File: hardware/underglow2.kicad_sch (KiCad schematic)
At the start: 1 part, among them J101 J_Delphi_Sicma_24

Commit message: Schematic progress
Signed-off-by: Connor Rigby <connorr@hey.com>
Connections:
- net CAN_H renamed CAN/CAN_H
- net CAN_L renamed CAN/CAN_L
- net DI_1 renamed Digital Input/DI_1
- net DI_2 renamed Digital Input/DI_2
- net DI_3 renamed Digital Input/DI_3
- net DI_4 renamed Digital Input/DI_4
- net IGNITION renamed Power/EN
- net PIXEL_1 renamed RGB/PIXEL_1
- net PIXEL_2 renamed RGB/PIXEL_2
- net RGB1_12V renamed RGB/RGB1_12V
- net RGB1_B renamed RGB/RGB1_B
- net RGB1_G renamed RGB/RGB1_G
- net RGB1_GND renamed RGB/RGB1_GND
- net RGB1_R renamed RGB/RGB1_R
- net RGB2_12V renamed RGB/RGB2_12V
- net RGB2_B renamed RGB/RGB2_B
- net RGB2_G renamed RGB/RGB2_G
- net RGB2_GND renamed RGB/RGB2_GND
- net RGB2_R renamed RGB/RGB2_R
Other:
- added sheet Application (Application.kicad_sch)
- added sheet BLE (BLE.kicad_sch)
- added sheet CAN (CAN.kicad_sch)
- added sheet Digital Input (Digital-Input.kicad_sch)
- added sheet RGB (RGB.kicad_sch)
- note added: "3V3 TTL Input"
- note added: "High Side Input"
- moved on the sheet: J101

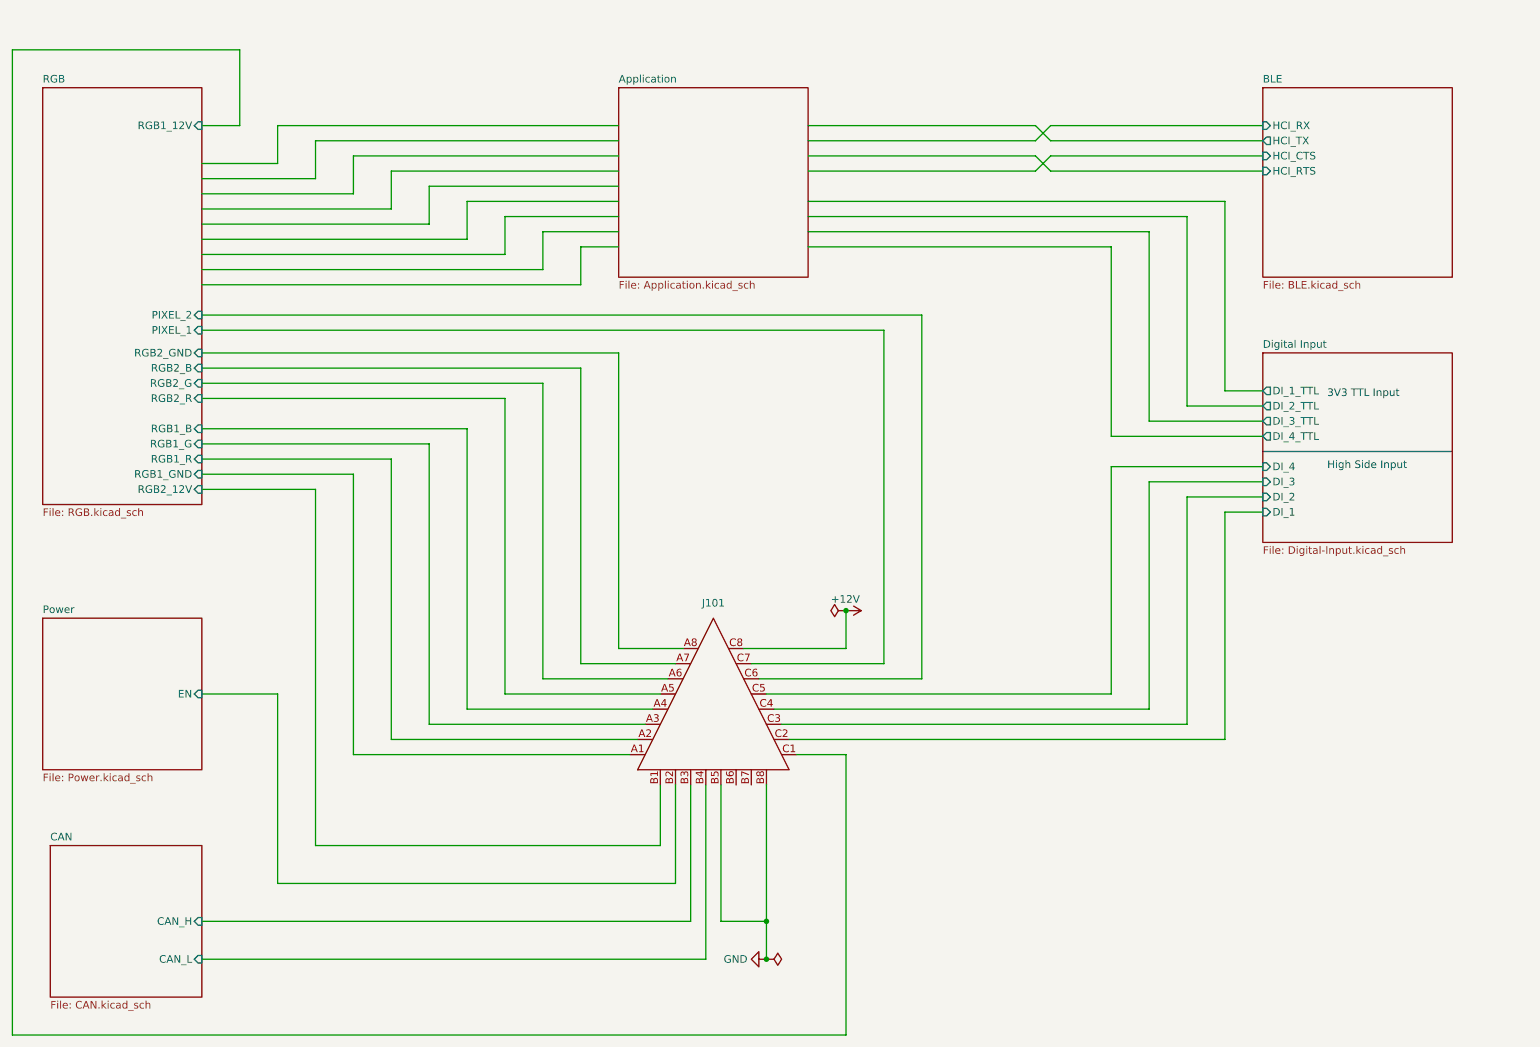
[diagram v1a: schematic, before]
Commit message: Schematic updates: stm32 sheet
Signed-off-by: Connor Rigby <connorr@hey.com>
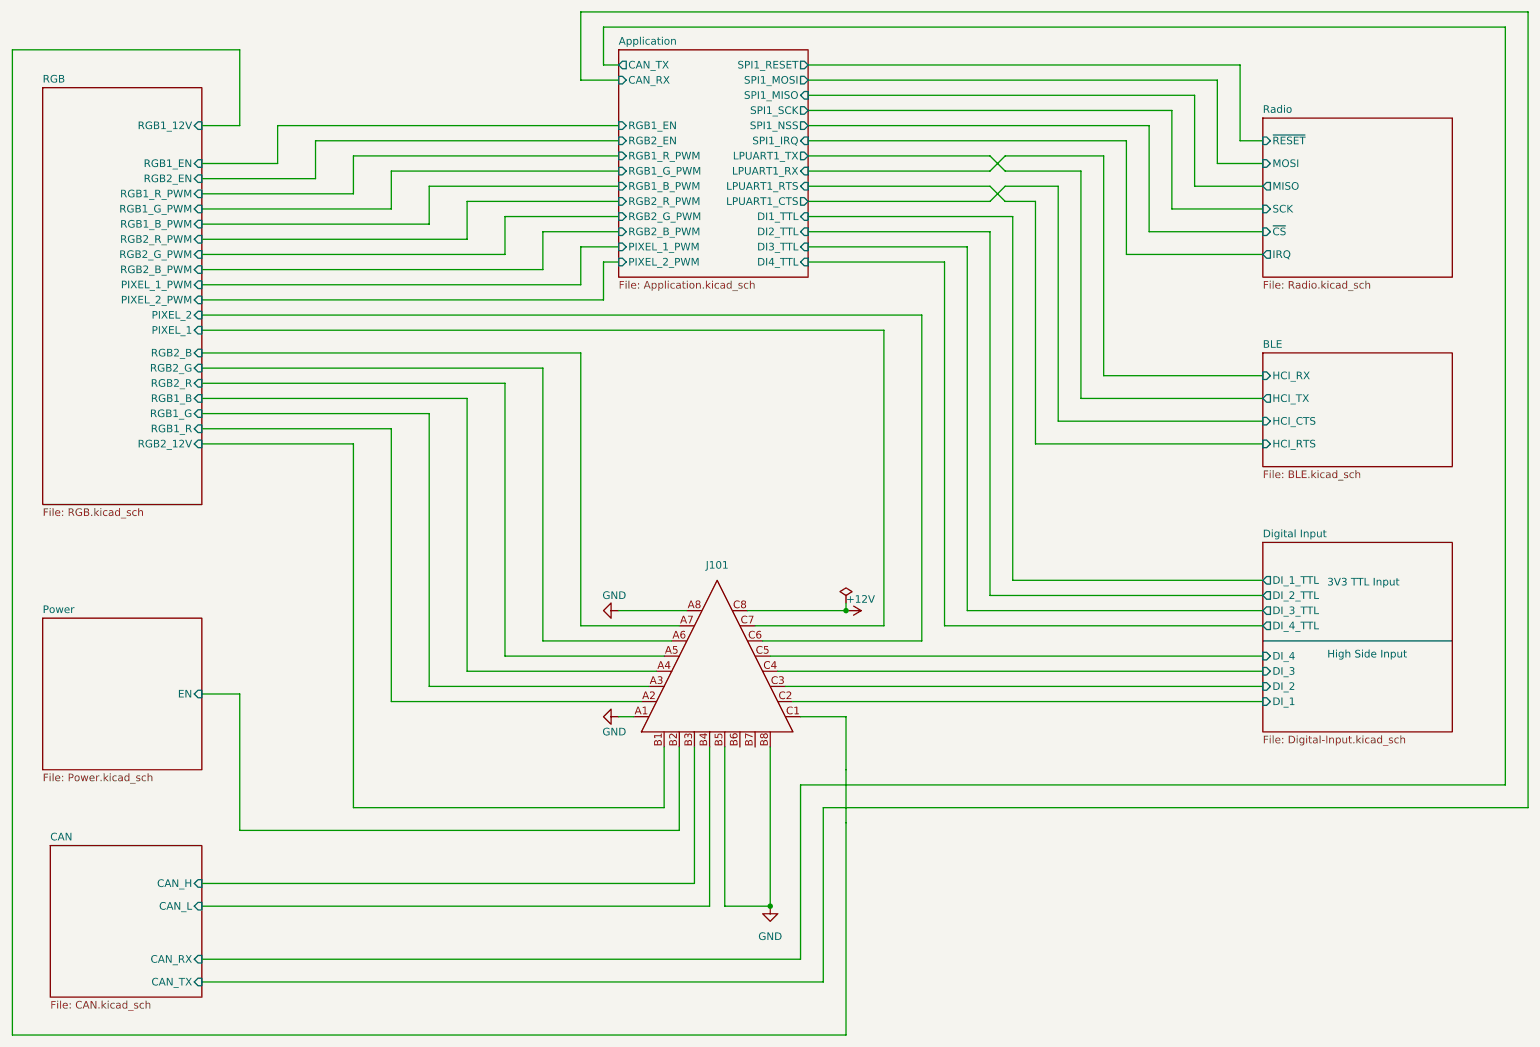
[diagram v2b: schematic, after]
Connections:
- net RGB/RGB1_GND is gone; now on net GND: J101.A1
- net RGB/RGB2_GND is gone; now on net GND: J101.A8
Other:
- added sheet Radio (Radio.kicad_sch)
- sheet Application ports: added CAN_RX, CAN_TX, DI1_TTL, DI2_TTL, DI3_TTL, DI4_TTL, LPUART1_CTS, LPUART1_RTS, LPUART1_RX, LPUART1_TX, PIXEL_1_PWM, PIXEL_2_PWM, RGB1_B_PWM, RGB1_EN, RGB1_G_PWM, RGB1_R_PWM, RGB2_B_PWM, RGB2_EN, RGB2_G_PWM, RGB2_R_PWM, SPI1_IRQ, SPI1_MISO, SPI1_MOSI, SPI1_NSS, SPI1_RESET, SPI1_SCK; removed none
- sheet CAN ports: added CAN_RX, CAN_TX; removed none
- sheet RGB ports: added PIXEL_1_PWM, PIXEL_2_PWM, RGB1_B_PWM, RGB1_EN, RGB1_G_PWM, RGB1_R_PWM, RGB2_B_PWM, RGB2_EN, RGB2_G_PWM, RGB2_R_PWM; removed RGB1_GND, RGB2_GND
- moved on the sheet: J101

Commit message: Almost ready for fab
Signed-off-by: Connor Rigby <connorr@hey.com>
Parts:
- J101: now left out of the parts list
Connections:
- no-connect marks 0 -> 2
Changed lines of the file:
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@@
 (kicad_sch (version 20230121) (generator eeschema)
   (paper "A4")
+  (junction (at 148.59 146.05) (diameter 0) (color 0 0 0 0)
+  )
   (junction (at 165.1 119.38) (diameter 0) (color 0 0 0 0)
   )
-  (junction (at 152.4 168.91) (diameter 0) (color 0 0 0 0)
-  )
+  (no_connect (at 147.32 142.24))
+  (no_connect (at 149.86 142.24))
   (wire (pts (xy 127 60.96) (xy 124.46 60.96))
     (stroke (width 0) (type default))
@@
     (stroke (width 0) (type default))
   )
+  (wire (pts (xy 148.59 146.05) (xy 148.59 147.32))
+    (stroke (width 0) (type default))
+  )
   (wire (pts (xy 204.47 83.82) (xy 234.95 83.82))
     (stroke (width 0) (type default))
@@
     (stroke (width 0) (type default))
   )
+  (wire (pts (xy 144.78 142.24) (xy 144.78 146.05))
+    (stroke (width 0) (type default))
+  )
+  (wire (pts (xy 152.4 146.05) (xy 148.59 146.05))
+    (stroke (width 0) (type default))
+  )
   (wire (pts (xy 57.15 69.85) (xy 177.8 69.85))
     (stroke (width 0) (type default))
@@
     (stroke (width 0) (type default))
   )
-  (wire (pts (xy 127 119.38) (xy 138.43 119.38))
-    (stroke (width 0) (type default))
-  )
   (wire (pts (xy 189.23 116.84) (xy 189.23 55.88))
     (stroke (width 0) (type default))
@@
     (stroke (width 0) (type default))
   )
-  (wire (pts (xy 127 137.16) (xy 129.54 137.16))
-    (stroke (width 0) (type default))
-  )
   (wire (pts (xy 88.9 134.62) (xy 130.81 134.62))
     (stroke (width 0) (type default))
@@
     (stroke (width 0) (type default))
   )
+  (wire (pts (xy 152.4 142.24) (xy 152.4 146.05))
+    (stroke (width 0) (type default))
+  )
   (wire (pts (xy 57.15 62.23) (xy 114.3 62.23))
     (stroke (width 0) (type default))
@@
   )
   (wire (pts (xy 114.3 78.74) (xy 57.15 78.74))
-    (stroke (width 0) (type default))
-  )
-  (wire (pts (xy 144.78 168.91) (xy 152.4 168.91))
     (stroke (width 0) (type default))
   )
@@
     (stroke (width 0) (type default))
   )
+  (wire (pts (xy 144.78 146.05) (xy 148.59 146.05))
+    (stroke (width 0) (type default))
+  )
   (wire (pts (xy 127 40.64) (xy 76.2 40.64))
     (stroke (width 0) (type default))
@@
     (stroke (width 0) (type default))
   )
-  (wire (pts (xy 144.78 142.24) (xy 144.78 168.91))
-    (stroke (width 0) (type default))
-  )
   (wire (pts (xy 120.65 58.42) (xy 120.65 64.77))
     (stroke (width 0) (type default))
@@
   )
   (wire (pts (xy 63.5 133.35) (xy 63.5 156.21))
-    (stroke (width 0) (type default))
-  )
-  (wire (pts (xy 152.4 142.24) (xy 152.4 168.91))
     (stroke (width 0) (type default))
   )
@@
   (text "High Side Input" (at 245.745 127.635 0)
     (effects (font (size 1.27 1.27)) (justify left bottom))
+  )
+  (symbol (lib_id "power:GND") (at 138.43 119.38 270) (unit 1)
+    (in_bom yes) (on_board yes) (dnp no) (fields_autoplaced)
+    (property "Reference" "#PWR0159" (at 132.08 119.38 0)
+      (effects (font (size 1.27 1.27)) hide)
+    )
+    (property "Value" "GND" (at 134.62 120.015 90)
+      (effects (font (size 1.27 1.27)) (justify right))
+    )
+    (property "Footprint" "" (at 138.43 119.38 0)
+      (effects (font (size 1.27 1.27)) hide)
+    )
+    (property "Datasheet" "" (at 138.43 119.38 0)
+      (effects (font (size 1.27 1.27)) hide)
+    )
+    (pin "1")
+    (instances
+      (project "underglow2"
+        (path "/dcbdf88a-d6ac-4b1d-9514-0b0ce113d90b/f6dd0682-1649-403c-b931-941640049f3a"
+          (reference "#PWR0159") (unit 1)
+        )
+        (path "/dcbdf88a-d6ac-4b1d-9514-0b0ce113d90b"
+          (reference "#PWR0105") (unit 1)
+        )
+      )
+    )
   )
   (symbol (lib_id "power:PWR_FLAG") (at 165.1 118.11 0) (unit 1)
@@
     )
   )
-  (symbol (lib_id "power:GND") (at 152.4 168.91 0) (unit 1)
+  (symbol (lib_id "power:GND") (at 129.54 137.16 270) (unit 1)
     (in_bom yes) (on_board yes) (dnp no) (fields_autoplaced)
-    (property "Reference" "#PWR0105" (at 152.4 175.26 0)
-      (effects (font (size 1.27 1.27)) hide)
-    )
-    (property "Value" "GND" (at 152.4 173.99 0)
-      (effects (font (size 1.27 1.27)))
-    )
-    (property "Footprint" "" (at 152.4 168.91 0)
-      (effects (font (size 1.27 1.27)) hide)
-    )
-    (property "Datasheet" "" (at 152.4 168.91 0)
+    (property "Reference" "#PWR0159" (at 123.19 137.16 0)
+      (effects (font (size 1.27 1.27)) hide)
+    )
+    (property "Value" "GND" (at 125.73 137.795 90)
+      (effects (font (size 1.27 1.27)) (justify right))
+    )
+    (property "Footprint" "" (at 129.54 137.16 0)
+      (effects (font (size 1.27 1.27)) hide)
+    )
+    (property "Datasheet" "" (at 129.54 137.16 0)
       (effects (font (size 1.27 1.27)) hide)
     )
@@
     (instances
       (project "underglow2"
+        (path "/dcbdf88a-d6ac-4b1d-9514-0b0ce113d90b/f6dd0682-1649-403c-b931-941640049f3a"
+          (reference "#PWR0159") (unit 1)
+        )
         (path "/dcbdf88a-d6ac-4b1d-9514-0b0ce113d90b"
-          (reference "#PWR0105") (unit 1)
+          (reference "#PWR0101") (unit 1)
         )
       )
     )
   )
-  (symbol (lib_name "GND_1") (lib_id "power:GND") (at 127 119.38 270) (unit 1)
-    (in_bom yes) (on_board yes) (dnp no)
-    (property "Reference" "#PWR0106" (at 120.65 119.38 0)
-      (effects (font (size 1.27 1.27)) hide)
-    )
-    (property "Value" "GND" (at 128.27 116.8399 90)
-      (effects (font (size 1.27 1.27)) (justify right))
-    )
-    (property "Footprint" "" (at 127 119.38 0)
-      (effects (font (size 1.27 1.27)) hide)
-    )
-    (property "Datasheet" "" (at 127 119.38 0)
-      (effects (font (size 1.27 1.27)) hide)
-    )
-    (pin "1")
-    (instances
-      (project "underglow2"
-        (path "/dcbdf88a-d6ac-4b1d-9514-0b0ce113d90b"
-          (reference "#PWR0106") (unit 1)
-        )
-      )
-    )
-  )
-  (symbol (lib_name "GND_1") (lib_id "power:GND") (at 127 137.16 270) (unit 1)
-    (in_bom yes) (on_board yes) (dnp no)
-    (property "Reference" "#PWR0108" (at 120.65 137.16 0)
-      (effects (font (size 1.27 1.27)) hide)
-    )
-    (property "Value" "GND" (at 128.27 139.6999 90)
-      (effects (font (size 1.27 1.27)) (justify right))
-    )
-    (property "Footprint" "" (at 127 137.16 0)
-      (effects (font (size 1.27 1.27)) hide)
-    )
-    (property "Datasheet" "" (at 127 137.16 0)
-      (effects (font (size 1.27 1.27)) hide)
-    )
-    (pin "1")
-    (instances
-      (project "underglow2"
-        (path "/dcbdf88a-d6ac-4b1d-9514-0b0ce113d90b"
-          (reference "#PWR0108") (unit 1)
-        )
-      )
-    )
-  )
   (symbol (lib_id "bom:J_Delphi_Sicma_24") (at 143.51 127 0) (unit 1)
-    (in_bom yes) (on_board yes) (dnp no)
+    (in_bom no) (on_board yes) (dnp no)
     (property "Reference" "J101" (at 143.51 111.76 0)
       (effects (font (size 1.27 1.27)))
@@
   )
   (symbol (lib_id "power:+12V") (at 165.1 119.38 270) (unit 1)
-    (in_bom yes) (on_board yes) (dnp no)
+    (in_bom yes) (on_board yes) (dnp no) (fields_autoplaced)
     (property "Reference" "#PWR0107" (at 161.29 119.38 0)
       (effects (font (size 1.27 1.27)) hide)
@@
         )
       )
+    )
+  )
+  (symbol (lib_id "power:GND") (at 148.59 147.32 0) (unit 1)
+    (in_bom yes) (on_board yes) (dnp no) (fields_autoplaced)
+    (property "Reference" "#PWR0159" (at 148.59 153.67 0)
+      (effects (font (size 1.27 1.27)) hide)
+    )
+    (property "Value" "GND" (at 148.59 152.4 0)
+      (effects (font (size 1.27 1.27)))
+    )
+    (property "Footprint" "" (at 148.59 147.32 0)
+      (effects (font (size 1.27 1.27)) hide)
+    )
+    (property "Datasheet" "" (at 148.59 147.32 0)
+      (effects (font (size 1.27 1.27)) hide)
+    )
+    (pin "1")
+    (instances
+      (project "underglow2"
+        (path "/dcbdf88a-d6ac-4b1d-9514-0b0ce113d90b/f6dd0682-1649-403c-b931-941640049f3a"
+          (reference "#PWR0159") (unit 1)
+        )
+        (path "/dcbdf88a-d6ac-4b1d-9514-0b0ce113d90b"
+          (reference "#PWR0106") (unit 1)
+        )
+      )

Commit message: Pre-production updates
Signed-off-by: Connor Rigby <connorr@hey.com>
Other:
- company: (none) -> https://cone.codes
- title: (none) -> coneRGB2
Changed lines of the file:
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@@
 (kicad_sch (version 20230121) (generator eeschema)
   (paper "A4")
+  (title_block
+    (title "coneRGB2")
+    (date "2023-03-20")
+    (rev "1")
+    (company "https://cone.codes")
+    (comment 1 "https://github.com/connorrigby/underglow2")
+    (comment 2 "Designed by Connor Rigby")
+    (comment 3 "2 channel, 8 output, 4 input automotive PMU with wirless syncing and BLE control")
+    (comment 4 "Automotive RGB and NZR controller")
+  )
   (junction (at 148.59 146.05) (diameter 0) (color 0 0 0 0)
   )
@@
     (stroke (width 0) (type default))
   )
+  (text_box "Main Connector\nCompatibility to be retained with V1 devices of the same connector\n"
+    (at 90.17 140.97 0) (size 36.83 7.62)
+    (stroke (width 0) (type default))
+    (fill (type none))
+    (effects (font (size 1.27 1.27)) (justify left top))
+  )
   (text "3V3 TTL Input" (at 245.745 115.57 0)
